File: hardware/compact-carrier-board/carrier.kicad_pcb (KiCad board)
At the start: 2 copper layers, 26 x 44 mm, 6 parts

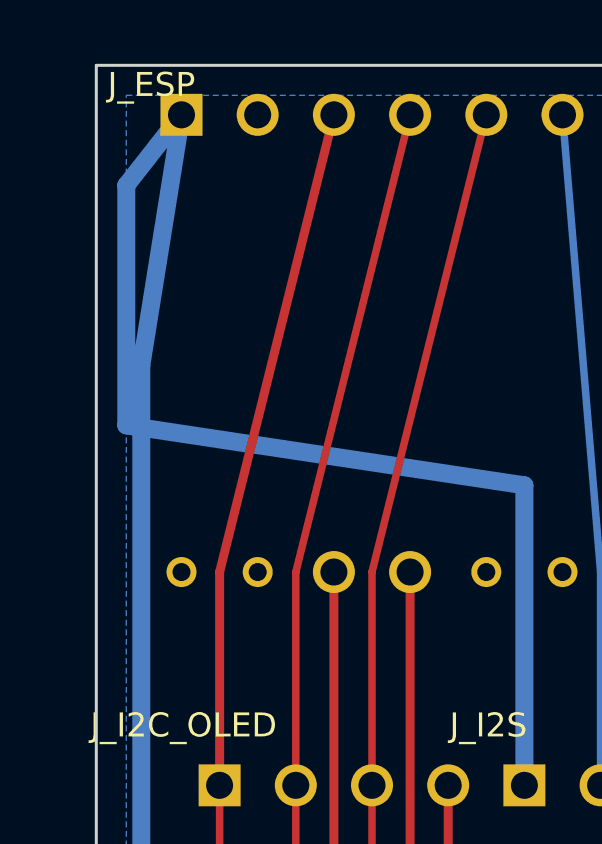
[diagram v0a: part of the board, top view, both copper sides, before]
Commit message: refactor(hardware): rename to compact-carrier-board; split ESP header into 2 designators
Rename per maintainer request (jamro, PR #32) to make room for multiple PCB
designs under hardware/. Also fixes JLC assembly quantity: the ESP socket was
one 18-pad footprint (J_ESP), so BOM/CPL quantity read as 1 despite needing
two physical 1x9 header strips. Split into J_ESP1 (row nearest USB-C) and
J_ESP2 (the other row, still carrying USB_DP/USB_DM on GPIO18/19) -- same
pads, positions, and nets, now two real designators. DRC still 0 errors, 0
unconnected. Gerbers diffed byte-for-byte identical except designator
attributes and emission order.

Co-Authored-By: Claude Sonnet 5 <noreply@anthropic.com>
Claude-Session: https://claude.ai/code/session_01NCfDjHNGeuiEoPta2KTLi3
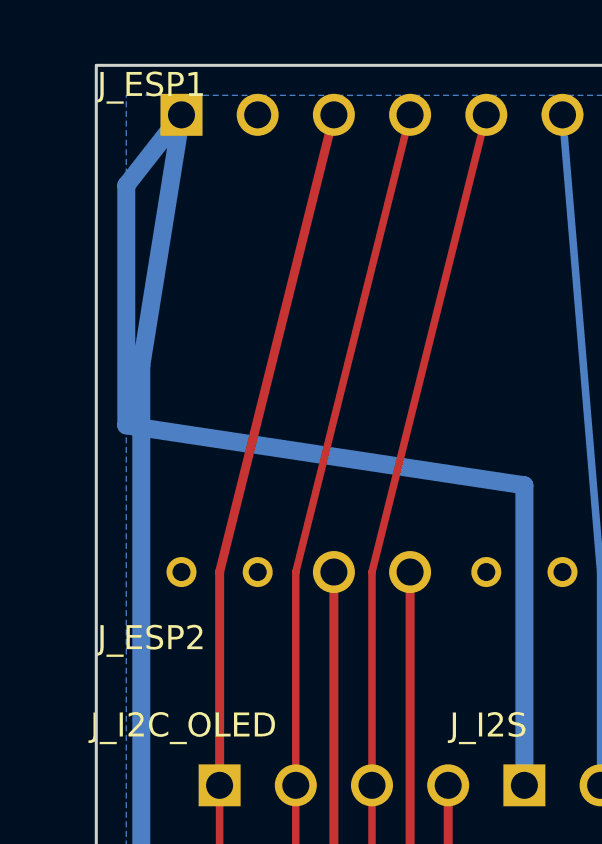
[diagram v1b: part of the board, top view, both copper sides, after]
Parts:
- removed J_ESP: , carrier:J_ESP
- added J_ESP1: , carrier:J_ESP1, F.Cu at (0.00, 0.00)
- added J_ESP2: , carrier:J_ESP2, F.Cu at (0.00, 0.00)
